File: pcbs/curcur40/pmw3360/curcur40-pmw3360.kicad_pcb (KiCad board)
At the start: 2 copper layers, 21.8 x 26.5 mm, 20 parts, among them J1 Conn_01x08, U1 PMW3360DM-T2QU, U2 TLV74318PDBVR

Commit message: fix error
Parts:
- moved TP3 20.6 mm to (154.9, 98.5)
- moved R3 20.0 mm to (144.0, 81.8), turned to 0 degrees
- moved TP1 8.91 mm to (154.9, 81.0)
- moved C3 1.66 mm to (138.0, 103.5), turned to 90 degrees
- moved TP2 1.43 mm to (147.2, 81.8)
- moved C4 0.40 mm to (147.6, 103.8)
- moved R4 0.30 mm to (153.5, 102.2), turned to 180 degrees
- moved R1 0.26 mm to (154.0, 85.5)
- moved R2 0.14 mm to (154.0, 83.5)
- moved C1 0.14 mm to (154.0, 94.3)
- moved C2 0.14 mm to (154.0, 96.0)
- turned C5 to 0 degrees
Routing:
- net GND: track 2.34 -> 49.3 mm, vias 10 -> 8
- net V_{IN}: track 51.5 -> 66.8 mm, vias 4 -> 2
- net V_{IO}: track 26.4 -> 14.7 mm
- net VDD: track 63.2 -> 51.5 mm, vias 5 -> 4
- net /MISO: track 35.0 -> 40.4 mm, vias 1 -> 2
- net Net-(U1-LED_P): track 20.1 -> 24.0 mm
- net /CS: track 6.71 -> 8.15 mm
- net Net-(U1-VDDPIX): track 5.30 -> 3.88 mm
- net /RESET: track 30.1 -> 31.3 mm
- net /MOSI: track 6.08 -> 6.73 mm
- removed copper zone on F.Cu, net GND
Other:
- board text removed: "${TITLE} Rev ${REVISION}"
- board text removed: "CS"
- board text removed: "GND"
- board text removed: "JP1: [1-2 3]V_{IO}=V_{IN} [1 2-3]V_{IO}=V_{DD}"
- board text removed: "MISO"
- board text removed: "MOSI"
- board text removed: "Motion"
- board text removed: "Reset"
- board text removed: "SCLK"
- board text removed: "V_{IN}"

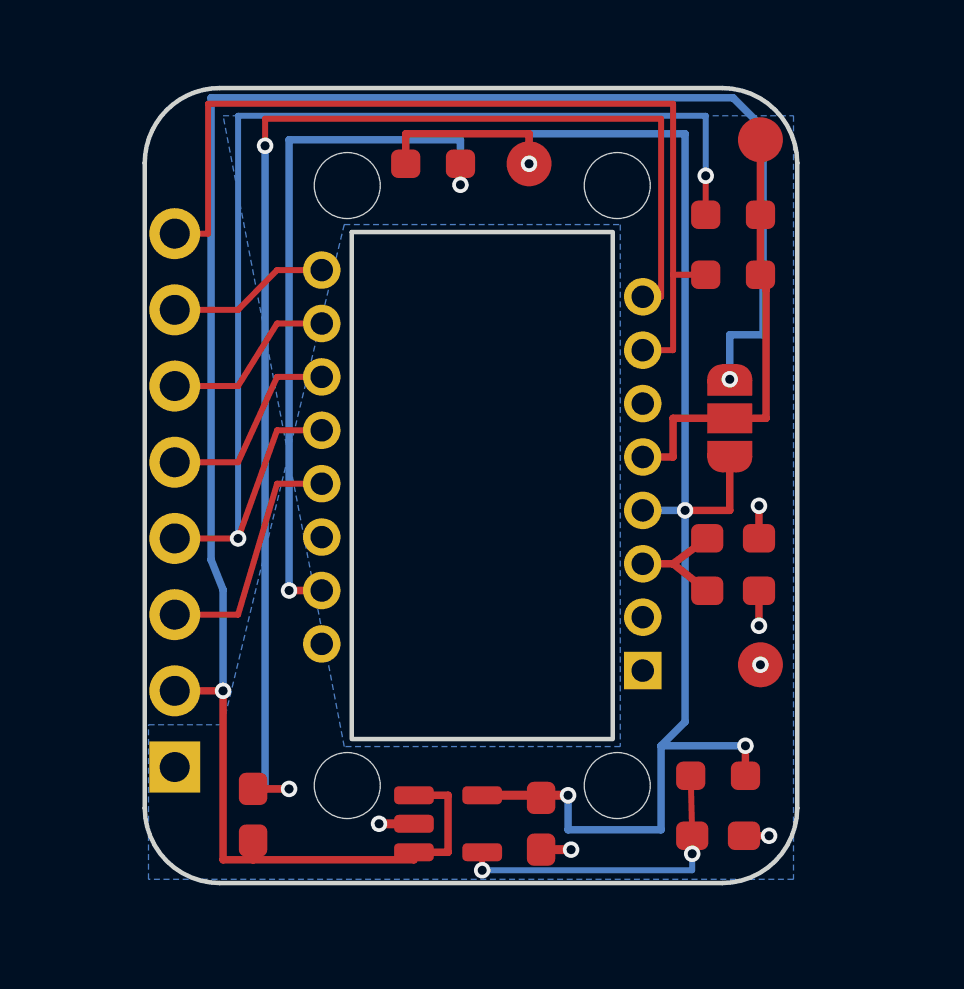
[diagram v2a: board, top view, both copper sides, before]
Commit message: 🔴 1. 致命的な不具合（Critical：物理的に組立不可、または動作不可）
[Critical-1] トラックボール部の3D機構・光学設計の破綻（4重の物理的干渉・焦点外れ）
[Critical-2] 左右メイン基板の取付穴径が ∅2.20 mm になっており、M2スペーサーが貫通できない
[Critical-3] 3Dプリントケース内部の 2.0mm スペーサー受けボスが消失しており、高さが 2.0 mm 合わない
[Critical-4] PMW3360 センサー基板のプルアップ抵抗 R1（10kΩ）が PCBA の BOM/CPL から除外されており、リセット端子（NRESET）がフローティング（不定）になる
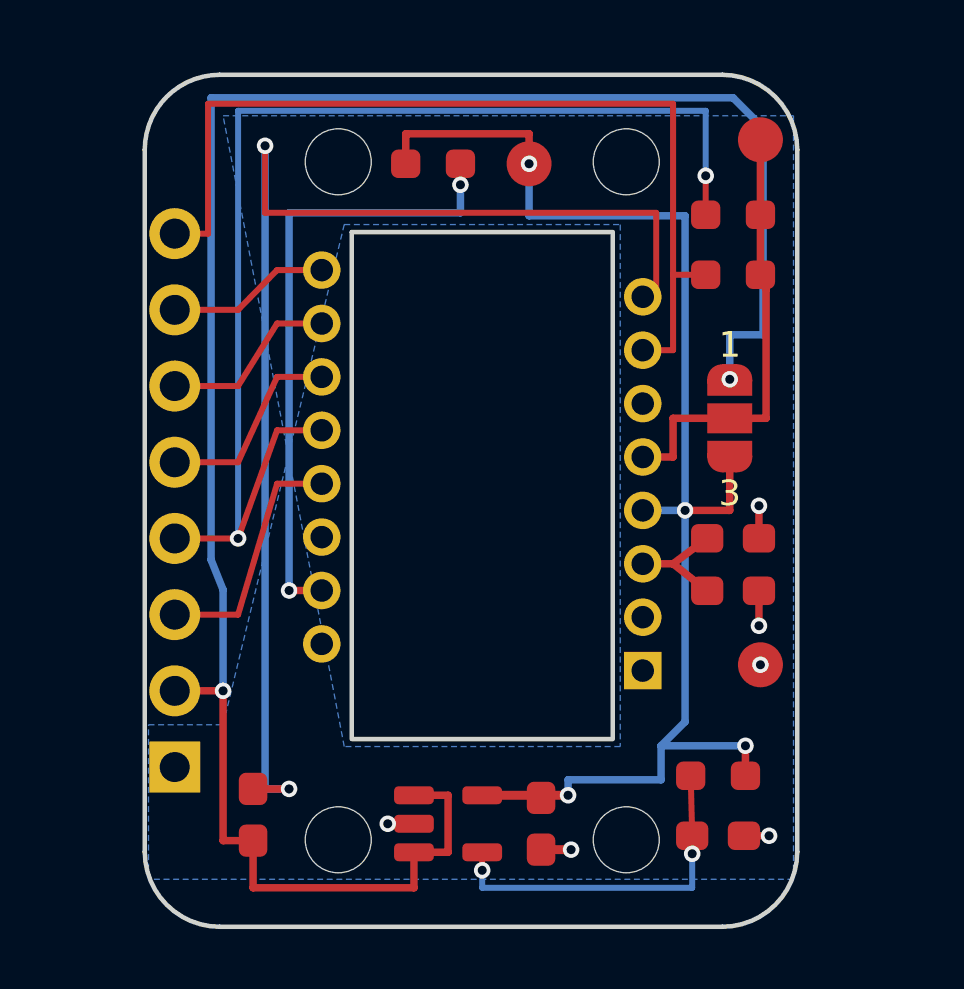
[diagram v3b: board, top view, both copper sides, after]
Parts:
- moved H3 1.83 mm to (140.8, 104.3)
- moved H4 1.83 mm to (150.4, 104.3)
- moved H1 0.85 mm to (140.8, 81.7)
- moved H2 0.85 mm to (150.4, 81.7)
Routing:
- net VDD: track 51.5 -> 47.2 mm
- net Net-(U1-LED_P): track 24.0 -> 21.0 mm
- net GND: track 49.3 -> 46.9 mm
- net V_{IN}: track 66.8 -> 68.1 mm
- net Net-(U2-NC): track 10.8 -> 11.9 mm
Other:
- board size 21.8 x 26.5 mm -> 21.8 x 28.4 mm
- board text added: "1"
- board text added: "3"
- board text added: "CK"
- board text added: "CS"
- board text added: "G"
- board text added: "MI"
- board text added: "MO"
- board text added: "V"

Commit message: mv trackball hole
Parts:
- moved H2 7.20 mm to (157.6, 81.7)
- moved H4 7.20 mm to (157.6, 104.3)
- moved H1 7.20 mm to (133.6, 81.7)
- moved H3 7.20 mm to (133.6, 104.3)
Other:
- board size 21.8 x 28.4 mm -> 28 x 28.4 mm
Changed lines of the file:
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@@
 		(duplicate_pad_numbers_are_jumpers no)
 		(fp_line
-			(start 1.8 19.55)
-			(end 1.8 -1.8)
-			(stroke
-				(width 0.05)
-				(type solid)
-			)
-			(layer "F.CrtYd")
-		)
-		(fp_line
-			(start 1.8 -1.8)
-			(end -1.8 -1.8)
-			(stroke
-				(width 0.05)
-				(type solid)
-			)
-			(layer "F.CrtYd")
-		)
-		(fp_line
-			(start -1.8 19.55)
-			(end 1.8 19.55)
-			(stroke
-				(width 0.05)
-				(type solid)
-			)
-			(layer "F.CrtYd")
-		)
-		(fp_line
-			(start -1.8 -1.8)
-			(end -1.8 19.55)
-			(stroke
-				(width 0.05)
-				(type solid)
-			)
-			(layer "F.CrtYd")
-		)
-		(fp_line
 			(start 1.27 19.05)
 			(end -1.27 19.05)
@@
 	(footprint "MountingHole_2.2mm_M2"
 		(layer "F.Cu")
-		(at 150.439 81.7338)
+		(at 157.639 81.7338)
 		(descr "Mounting Hole 2.2mm, M2, no annular, generated by kicad-footprint-generator mountinghole.py")
 		(tags "mountinghole M2")
@@
 			(layer "Cmts.User")
 		)
-		(fp_circle
-			(center 0 0)
-			(end 1.2 0)
-			(stroke
-				(width 0.05)
-				(type solid)
-			)
-			(fill no)
-			(layer "F.CrtYd")
-		)
 		(fp_text user "${REFERENCE}"
 			(at 0 0 0)
@@
 	(footprint "MountingHole_2.2mm_M2"
 		(layer "F.Cu")
-		(at 150.439 104.3338)
+		(at 157.639 104.3338)
 		(descr "Mounting Hole 2.2mm, M2, no annular, generated by kicad-footprint-generator mountinghole.py")
 		(tags "mountinghole M2")
@@
 			(layer "Cmts.User")
 		)
-		(fp_circle
-			(center 0 0)
-			(end 1.2 0)
-			(stroke
-				(width 0.05)
-				(type solid)
-			)
-			(fill no)
-			(layer "F.CrtYd")
-		)
 		(fp_text user "${REFERENCE}"
 			(at 0 0 0)
@@
 	(footprint "MountingHole_2.2mm_M2"
 		(layer "F.Cu")
-		(at 140.839 81.7338)
+		(at 133.639 81.7338)
 		(descr "Mounting Hole 2.2mm, M2, no annular, generated by kicad-footprint-generator mountinghole.py")
 		(tags "mountinghole M2")
@@
 			(layer "Cmts.User")
 		)
-		(fp_circle
-			(center 0 0)
-			(end 1.2 0)
-			(stroke
-				(width 0.05)
-				(type solid)
-			)
-			(fill no)
-			(layer "F.CrtYd")
-		)
 		(fp_text user "${REFERENCE}"
 			(at 0 0 0)
@@
 	(footprint "MountingHole_2.2mm_M2"
 		(layer "F.Cu")
-		(at 140.839 104.3338)
+		(at 133.639 104.3338)
 		(descr "Mounting Hole 2.2mm, M2, no annular, generated by kicad-footprint-generator mountinghole.py")
 		(tags "mountinghole M2")
@@
 			(layer "Cmts.User")
 		)
-		(fp_circle
-			(center 0 0)
-			(end 1.2 0)
-			(stroke
-				(width 0.05)
-				(type solid)
-			)
-			(fill no)
-			(layer "F.CrtYd")
-		)
 		(fp_text user "${REFERENCE}"
 			(at 0 0 0)
@@
 	)
 	(gr_arc
-		(start 134.389 81.3338)
-		(mid 135.121233 79.566033)
-		(end 136.889 78.8338)
+		(start 131.639 81.0338)
+		(mid 132.283365 79.478165)
+		(end 133.839 78.8338)
 		(stroke
 			(width 0.15)
@@
 	)
 	(gr_line
-		(start 134.389 104.7338)
-		(end 134.389 81.3338)
+		(start 131.639 105.0338)
+		(end 131.639 81.0338)
 		(stroke
 			(width 0.15)
@@
 	)
 	(gr_line
-		(start 136.889 78.8338)
-		(end 153.639 78.8338)
+		(start 133.839 78.8338)
+		(end 157.439 78.8338)
 		(stroke
 			(width 0.15)
@@
 	)
 	(gr_arc
-		(start 136.889 107.2338)
-		(mid 135.121233 106.501566)
-		(end 134.389 104.7338)
+		(start 133.839 107.2338)
+		(mid 132.283365 106.589434)
+		(end 131.639 105.0338)
 		(stroke
 			(width 0.15)
@@
 	)
 	(gr_arc
-		(start 153.639 78.8338)
-		(mid 155.406766 79.566033)
-		(end 156.139 81.3338)
+		(start 157.439 78.8338)
+		(mid 158.994634 79.478165)
+		(end 159.639 81.0338)
 		(stroke
 			(width 0.15)
@@
 	)
 	(gr_line
-		(start 153.639 107.2338)
-		(end 136.889 107.2338)
+		(start 157.439 107.2338)
+		(end 133.839 107.2338)
 		(stroke
 			(width 0.15)
@@
 	)
 	(gr_line
-		(start 156.139 81.3338)
-		(end 156.139 104.7338)
+		(start 159.639 81.0338)
+		(end 159.639 105.0338)
 		(stroke
 			(width 0.15)
@@
 	)
 	(gr_arc
-		(start 156.139 104.7338)
-		(mid 155.406766 106.501566)
-		(end 153.639 107.2338)
+		(start 159.639 105.0338)
+		(mid 158.994634 106.589434)
+		(end 157.439 107.2338)
 		(stroke
 			(width 0.15)
@@
 		(polygon
 			(pts
-				(xy 137 80.2) (xy 156.014 80.2) (xy 156.014 105.6508) (xy 134.513999 105.6508) (xy 134.513999 100.5)
-				(xy 137 100.5) (xy 141.039 83.8258) (xy 150.239 83.8258) (xy 150.239 101.2258) (xy 141.039 101.2258)
+				(xy 131.939 79.1338) (xy 159.339 79.1338) (xy 159.339 106.9338) (xy 131.939 106.9338)
 			)
 		)
